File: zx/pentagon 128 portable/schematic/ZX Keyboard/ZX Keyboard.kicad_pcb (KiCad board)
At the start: 2 copper layers, 48 parts, among them IC1 SN74LS245DW, IC2 SN74LS27N, IC3 SN74LS245DW

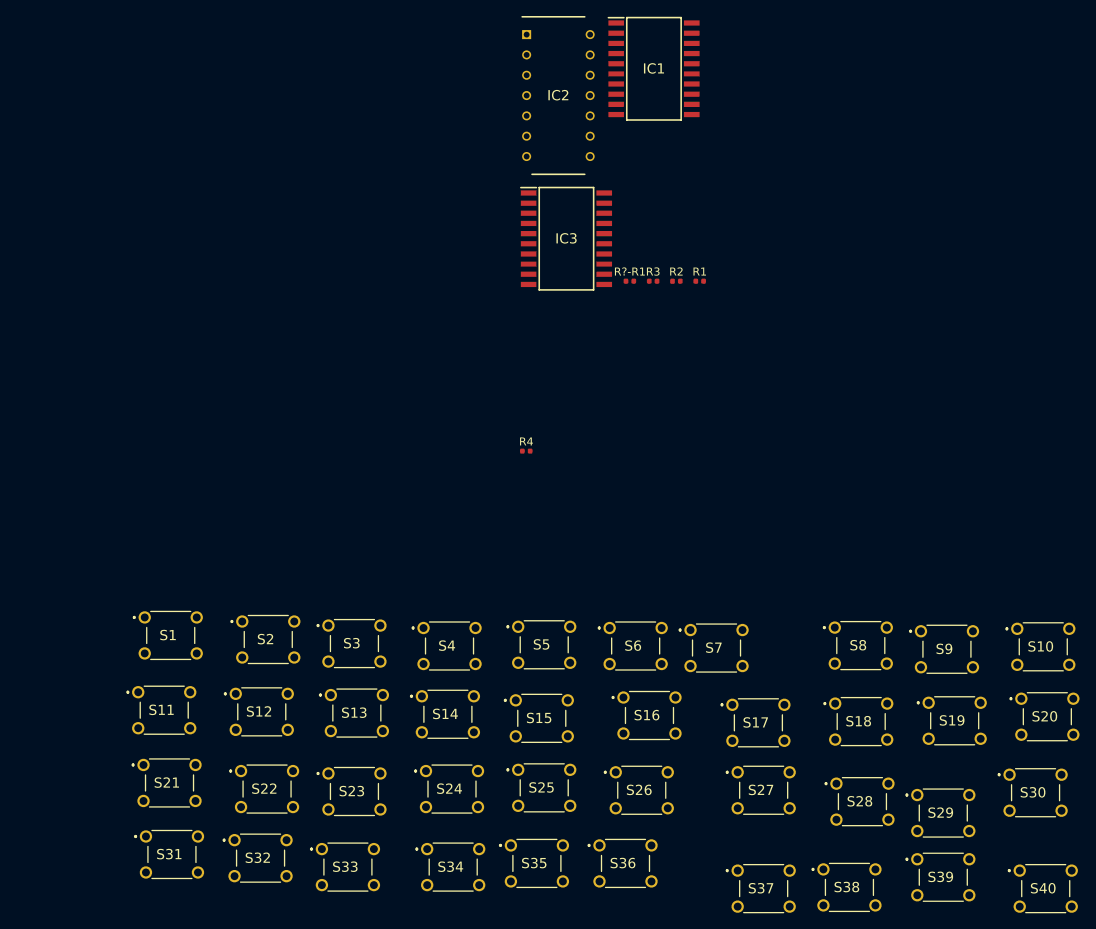
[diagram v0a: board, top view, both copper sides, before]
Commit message: reorganizing. finished ram and keyboard, updated z80
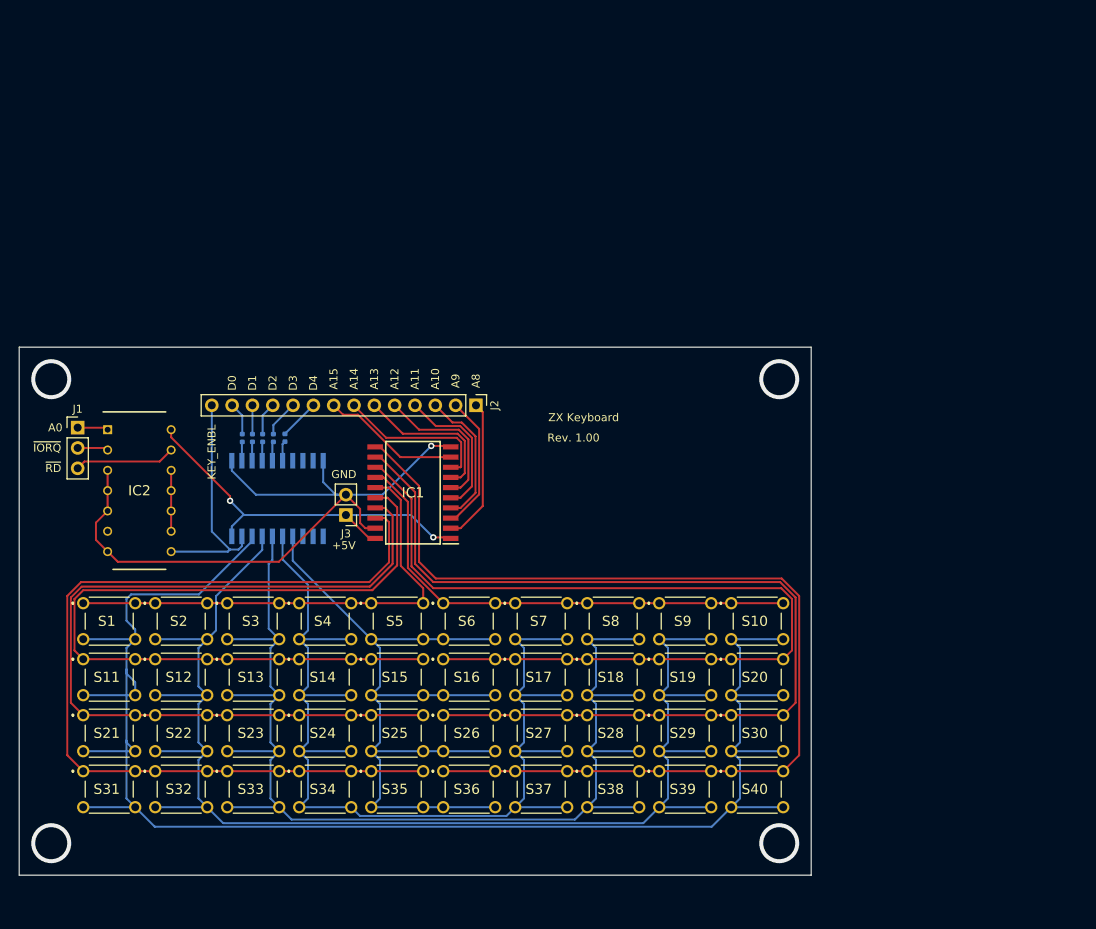
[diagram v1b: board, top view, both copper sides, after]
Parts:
- added J1: Conn_01x03, Connector_PinHeader_2.54mm:PinHeader_1x03_P2.54mm_Vertical, F.Cu at (35.3, 83.1)
- added J2: Conn_01x14, Connector_PinHeader_2.54mm:PinHeader_1x14_P2.54mm_Vertical, F.Cu at (85.1, 80.3)
- added J3: Conn_01x02, Connector_PinHeader_2.54mm:PinHeader_1x02_P2.54mm_Vertical, F.Cu at (68.8, 94.0)
- IC3, R1, R2, R3, R4, R?-R1: moved to B.Cu
- moved IC2 72.0 mm to (43.0, 90.9)
- moved IC1 60.9 mm to (77.2, 91.2), turned to 180 degrees
- moved R1 59.2 mm to (57.1, 84.4), turned to 90 degrees
- moved R2 55.3 mm to (58.4, 84.4), turned to 90 degrees
- moved R?-R1 52.3 mm to (55.9, 84.4), turned to 90 degrees
- moved R3 51.4 mm to (59.8, 84.4), turned to 90 degrees
- moved IC3 48.6 mm to (60.3, 91.9), turned to 270 degrees
- moved S40 38.1 mm to (117.0, 126.0)
- moved S20 36.6 mm to (117.0, 112.0)
- moved S10 35.9 mm to (117.0, 105.0)
- moved S30 35.6 mm to (117.0, 119.0)
- moved S19 34.1 mm to (108.0, 112.0)
- moved S39 34.1 mm to (108.0, 126.0)
- moved S29 33.8 mm to (108.0, 119.0)
- moved S9 32.9 mm to (108.0, 105.0)
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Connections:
- IC1 pad 2: (no net) -> /A8
- IC1 pad 3: (no net) -> /A9
- IC1 pad 4: (no net) -> /A10
- IC1 pad 5: (no net) -> /A11
- IC1 pad 6: (no net) -> /A12
- IC1 pad 7: (no net) -> /A13
- IC1 pad 8: (no net) -> /A14
- IC1 pad 9: (no net) -> /A15
- IC2 pad 1: (no net) -> /A0
- IC2 pad 13: (no net) -> /~RD
- IC2 pad 2: (no net) -> /~IORQ
- IC2 pad 3: (no net) -> GND
- IC2 pad 4: (no net) -> GND
- IC2 pad 5: (no net) -> GND
- R1 pad 2: (no net) -> /D1
- R2 pad 2: (no net) -> /D2
- R3 pad 2: (no net) -> /D3
- R4 pad 2: (no net) -> /D4
- R?-R1 pad 2: (no net) -> /D0
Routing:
- net /K_D0: track 0.00 -> 204.4 mm
- net /K_D1: track 0.00 -> 173.3 mm
- net /K_D2: track 0.00 -> 152.8 mm
- net /K_D3: track 0.00 -> 135.5 mm
- net /K_A15: track 0.00 -> 131.5 mm
- net /K_A14: track 0.00 -> 122.9 mm
- net /K_A13: track 0.00 -> 114.4 mm
- net /K_A8: track 0.00 -> 114.2 mm
- net /K_A9: track 0.00 -> 108.4 mm
- net /K_A10: track 0.00 -> 103.1 mm
- net /K_D4: track 0.00 -> 102.6 mm
- net GND: track 0.00 -> 89.2 mm, vias 0 -> 1
- net /K_A12: track 0.00 -> 62.4 mm
- net /K_A11: track 0.00 -> 60.4 mm
- net +5V: track 0.00 -> 49.7 mm, vias 0 -> 2
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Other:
- board outline added: 99 x 66 mm
- board text added: "+5V"
- board text added: "A0"
- board text added: "A10"
- board text added: "A11"
- board text added: "A12"
- board text added: "A13"
- board text added: "A14"
- board text added: "A15"
- board text added: "A8"
- board text added: "A9"
- board text added: "D0"
- board text added: "D1"
- board text added: "D2"
- board text added: "D3"
- board text added: "D4"
- board text added: "GND"
- board text added: "KEY_ENBL"
- board text added: "Rev. 1.00"
- board text added: "ZX Keyboard"
- board text added: "~IORQ"
- board text added: "~RD"
